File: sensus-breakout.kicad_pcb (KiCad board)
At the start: 2 copper layers, 14.1 x 33.1 mm, 7 parts, among them J1 v1 connector, J2 Breakout, J3 JLink, J5 USB_B_Micro, U1 XC6206P332MR

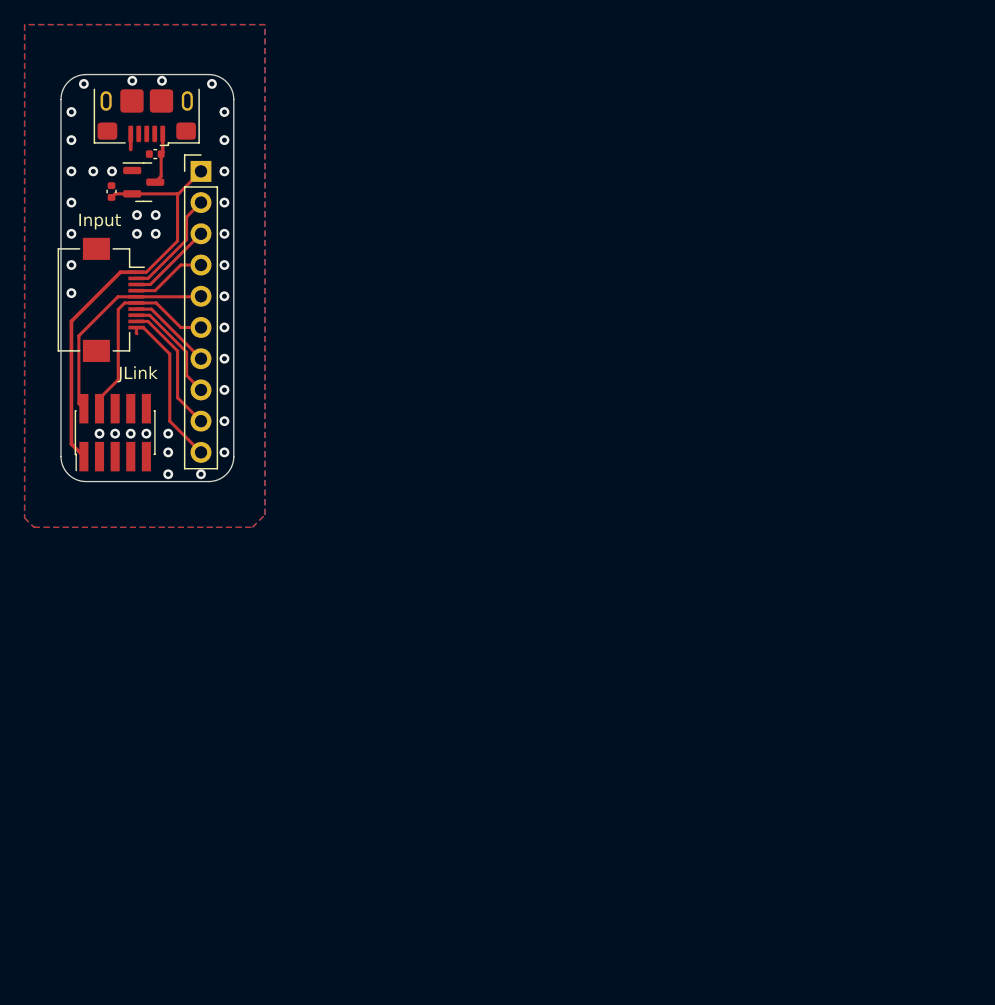
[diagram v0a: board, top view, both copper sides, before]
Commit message: Ordered second version of breakout board.
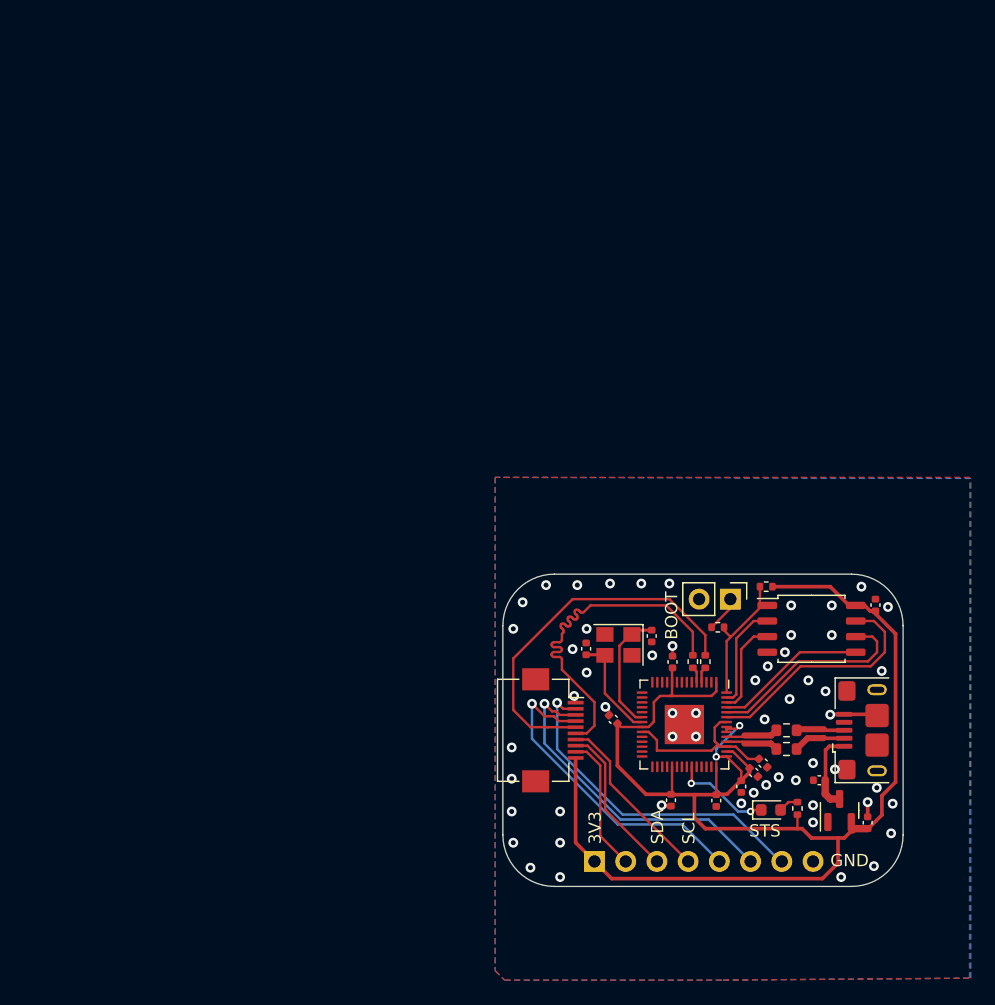
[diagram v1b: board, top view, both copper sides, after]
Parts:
- added C10: 1u, Capacitor_SMD:C_0402_1005Metric, F.Cu at (151.5, 108.1)
- added C11: 1u, Capacitor_SMD:C_0402_1005Metric, F.Cu at (150.7, 108.8)
- added C12: 100n, Capacitor_SMD:C_0402_1005Metric, F.Cu at (144.1, 99.8)
- added C3: 100n, Capacitor_SMD:C_0402_1005Metric, F.Cu at (160.7, 95.2)
- added C4: 30p, Capacitor_SMD:C_0402_1005Metric, F.Cu at (142.5, 97.7)
- added C5: 30p, Capacitor_SMD:C_0402_1005Metric, F.Cu at (137.1, 98.8)
- added C6: 100n, Capacitor_SMD:C_0402_1005Metric, F.Cu at (144.0, 111.1)
- added C7: 100n, Capacitor_SMD:C_0402_1005Metric, F.Cu at (147.7, 111.1)
- added C8: 100n, Capacitor_SMD:C_0402_1005Metric, F.Cu at (149.7, 110.0)
- added C9: 100n, Capacitor_SMD:C_0402_1005Metric, F.Cu at (139.3, 104.5)
- added D1: LED_Small, LED_SMD:LED_0603_1608Metric, F.Cu at (152.1, 111.9)
- added R1: 27, Resistor_SMD:R_0603_1608Metric, F.Cu at (153.4, 105.4)
- added R2: 27, Resistor_SMD:R_0603_1608Metric, F.Cu at (153.4, 106.9)
- added R3: 1k, Resistor_SMD:R_0402_1005Metric, F.Cu at (147.8, 97.0)
- added R4: 10k, Resistor_SMD:R_0402_1005Metric, F.Cu at (151.8, 93.7)
- added R5: 100, Resistor_SMD:R_0402_1005Metric, F.Cu at (146.8, 99.8)
- added R6: 100, Resistor_SMD:R_0402_1005Metric, F.Cu at (145.8, 99.8)
- added R7: 1k, Resistor_SMD:R_0402_1005Metric, F.Cu at (154.3, 111.8)
- added U2: RP2040, Package_DFN_QFN:QFN-56-1EP_7x7mm_P0.4mm_EP3.2x3.2mm, F.Cu at (145.1, 104.9)
- added U3: W25Q128JVS, Package_SO:SOIC-8_5.23x5.23mm_P1.27mm, F.Cu at (155.4, 97.2)
- added Y1: 12MHz, Crystal:Crystal_SMD_3225-4Pin_3.2x2.5mm, F.Cu at (139.7, 98.5)
- J2: value Breakout -> USB_BOOT; footprint Connector_PinHeader_2.54mm:PinHeader_1x10_P2.54mm_Vertical -> Connector_PinHeader_2.54mm:PinHeader_1x02_P2.54mm_Vertical
- J3: value JLink -> Conn_01x08; footprint Connector_PinHeader_1.27mm:PinHeader_2x05_P1.27mm_Vertical_SMD -> Connector_PinHeader_2.54mm:PinHeader_1x08_P2.54mm_Vertical; moved to B.Cu
- moved C2 80.1 mm to (160.0, 112.9)
- moved J5 78.4 mm to (160.8, 105.4), turned to 90 degrees
- moved U1 76.3 mm to (157.7, 111.9), turned to 90 degrees
- moved C1 74.2 mm to (156.1, 109.5)
- moved J2 55.4 mm to (148.8, 94.7), turned to -90 degrees
- moved J3 52.3 mm to (137.8, 116.1), turned to -90 degrees
- moved J1 50.0 mm to (134.4, 105.4)
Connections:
- J1 pad 1: +3.3V -> GND
- J1 pad 10: GND -> +3.3V
- J1 pad 5: /SWDIO -> /SWCLK
- J1 pad 6: /SWCLK -> /SWDIO
- J2 pad 1: +3.3V -> Net-(J2-Pin_1)
- J2 pad 2: Net-(J1-Pin_2) -> GND
- J3 pad 2: /SWDIO -> Net-(J1-Pin_9)
- J3 pad 3: GND -> Net-(J1-Pin_8)
- J3 pad 4: /SWCLK -> Net-(J1-Pin_7)
- J3 pad 5: GND -> Net-(J1-Pin_4)
- J3 pad 6: unconnected-(J3-Pin_6-Pad6) -> Net-(J1-Pin_3)
- J3 pad 7: unconnected-(J3-Pin_7-Pad7) -> Net-(J1-Pin_2)
- J3 pad 8: unconnected-(J3-Pin_8-Pad8) -> GND
- J5 pad 2: unconnected-(J5-D--Pad2) -> /USB_N
- J5 pad 3: unconnected-(J5-D+-Pad3) -> /USB_P
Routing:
- net +3.3V: track 34.8 -> 123.7 mm, vias 0 -> 2
- net Net-(J1-Pin_4): track 6.12 -> 26.4 mm, vias 0 -> 1
- net Net-(J1-Pin_3): track 6.97 -> 26.9 mm, vias 0 -> 1
- net Net-(U2-QSPI_SD3): track 0.00 -> 19.4 mm
- net Net-(J1-Pin_2): track 8.90 -> 27.5 mm, vias 0 -> 1
- net /QCLK: track 0.00 -> 17.0 mm
- net +1V1: track 0.00 -> 14.0 mm
- net /SWCLK: track 16.5 -> 30.3 mm
- net /SWDIO: track 17.4 -> 29.8 mm
- net Net-(U2-QSPI_SD0): track 0.00 -> 12.4 mm
- net Net-(U2-QSPI_SS): track 0.00 -> 11.8 mm
- net Net-(U2-XIN): track 0.00 -> 10.0 mm
- net Net-(U2-XOUT): track 0.00 -> 8.63 mm
- net Net-(U2-QSPI_SD1): track 0.00 -> 8.54 mm
- net /STS: track 0.00 -> 8.06 mm, vias 0 -> 2
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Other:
- board size 14.1 x 33.1 mm -> 32.6 x 25.4 mm
- board text added: "3V3"
- board text added: "BOOT"
- board text added: "GND"
- board text added: "Klausenprobe"
- board text added: "SCL"
- board text added: "SDA"
- board text added: "STS"
- board text removed: "Input"
- board text removed: "JLink"
